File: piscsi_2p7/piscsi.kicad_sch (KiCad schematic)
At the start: 88 parts, among them IC1 SN74LS641-1DW, IC2 SN74LS641-1DW, IC3 SN74LS641-1DW, IC4 SN74LS641-1DW, J1 Raspberry_Pi_2_3, J2 DNP, J4 I2C Pinout, J5 DNP, J6 CONNFLY DB-25, X1 Mac, X2 Dogcow, X3 Mac, X4 Dogcow, X5 Dogcow, X6 Dogcow, X7 Pi, X8 Pi

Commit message: as ordered 2.7
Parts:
- added C1, C2, C3, C4: 10uF, Capacitor_SMD:C_0402_1005Metric, symbol Device:C_Small
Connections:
- net +3V3: now also IC1.20 (VCC), IC2.20 (VCC), IC3.20 (VCC), IC4.20 (VCC), C1.1, C2.1, C3.1, C4.1
- net +5V: no longer IC1.20 (VCC), IC2.20 (VCC), IC3.20 (VCC), IC4.20 (VCC)
- net GND: now also C1.2, C2.2, C3.2, C4.2

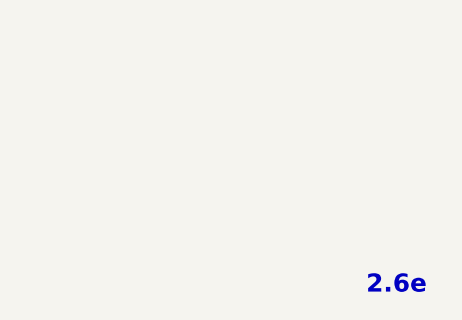
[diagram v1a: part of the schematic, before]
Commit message: regenerate schematic and convert to KiCad 7
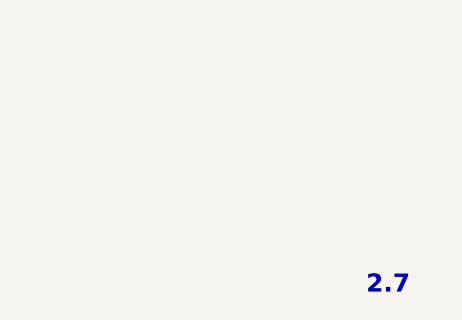
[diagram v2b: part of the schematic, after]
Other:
- note added: "2.7"
- note removed: "2.6e"
